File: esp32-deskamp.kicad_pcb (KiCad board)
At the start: 2 copper layers, 140.2 x 66.5 mm, 39 parts, among them J1 INPUT 00, J10 ADDITIONAL GPIO, J2 INPUT 01, J3 MUTE, J4 SLEEP, J5 PRE OUT, J6 LFE OUT, J7 INPUT SELECT, J8 MOTOR, J9 12V IN, K1 INPUT 00, K2 INPUT 01, K3 AMP MUTE, K4 AMP SLEEP, U1 ESP32 D1 MINI, U2 TSR 1-2433, U3 L9110, U4 ULN2003A

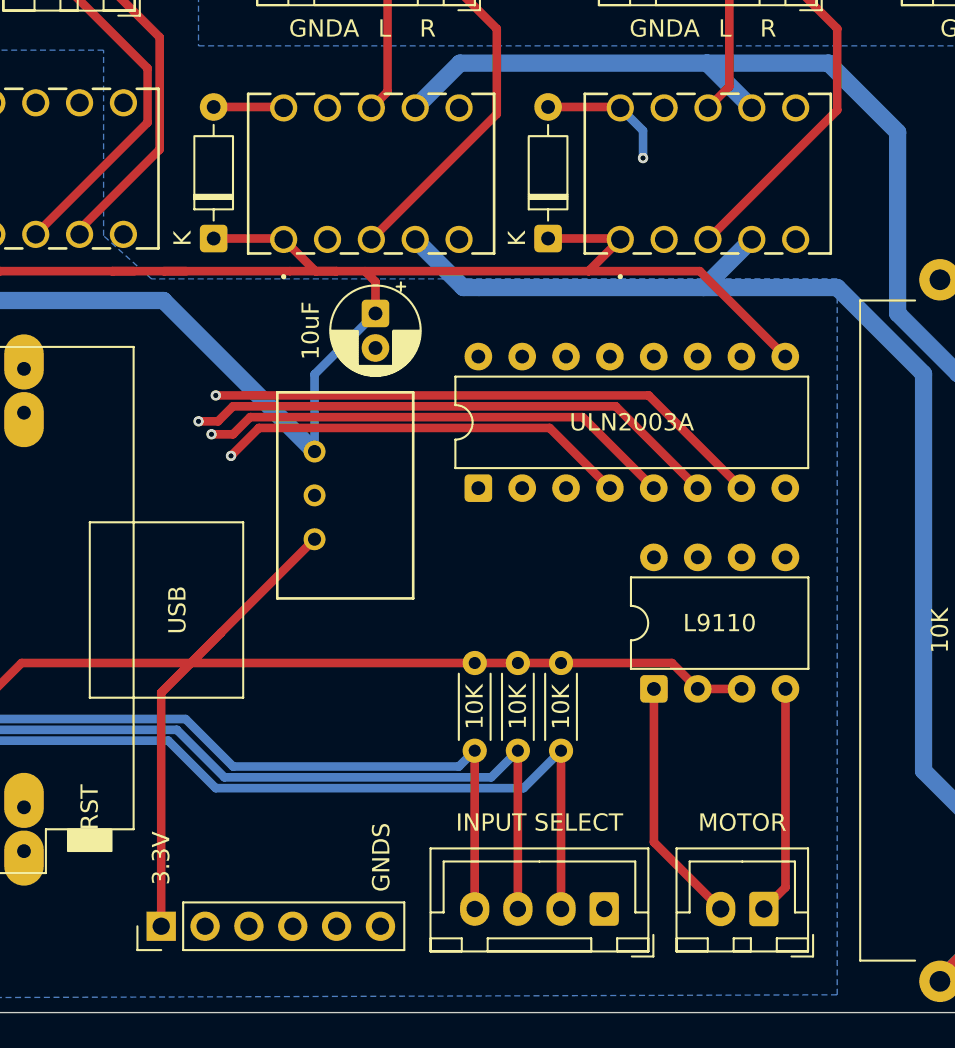
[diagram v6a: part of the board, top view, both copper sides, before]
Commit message: No surprise, more routing (relays)
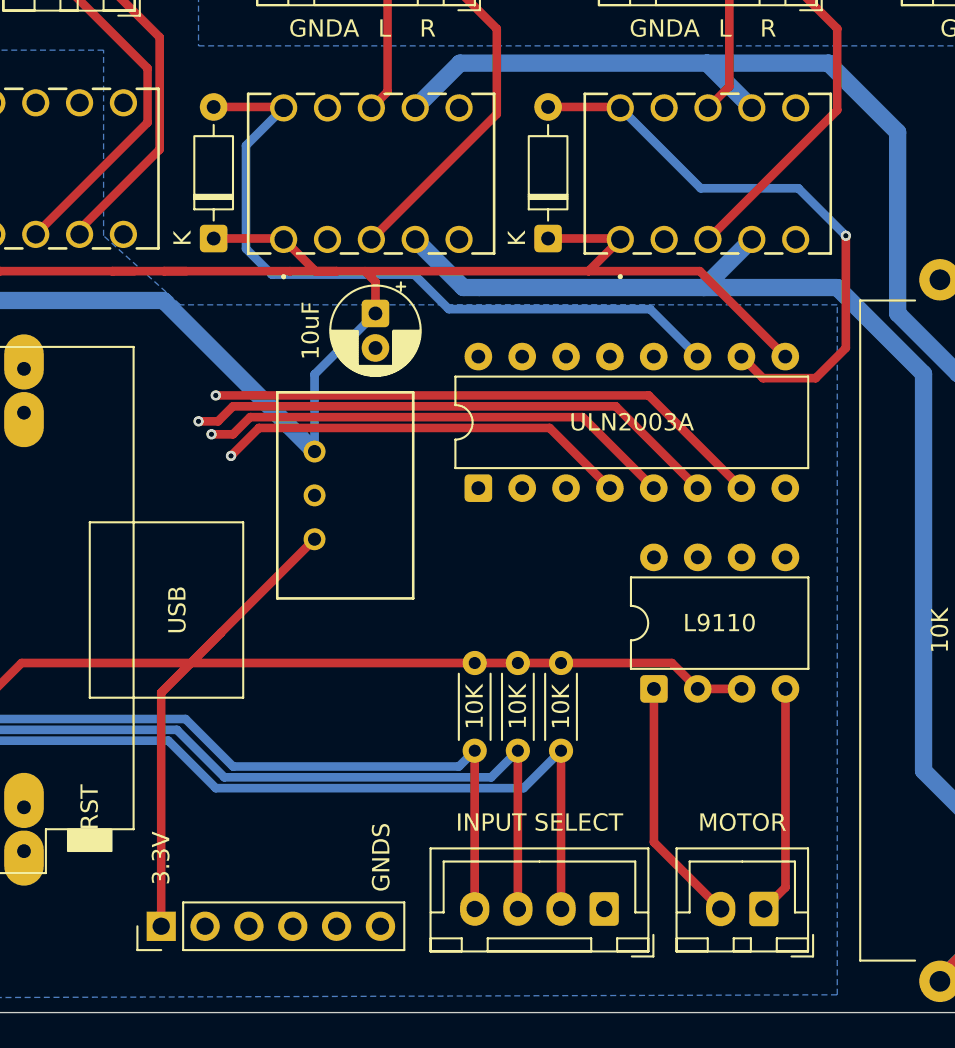
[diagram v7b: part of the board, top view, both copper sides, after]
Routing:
- net Relay0: track 4.00 -> 41.8 mm
- net Relay1: track 7.58 -> 34.1 mm
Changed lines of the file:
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@@
+	)
+	(segment
+		(start 145.5 57.25)
+		(end 147.5 59.25)
+		(width 0.5)
+		(layer "B.Cu")
+		(net 1)
+	)
+	(segment
+		(start 147.5 59.25)
+		(end 159.16 59.25)
+		(width 0.5)
+		(layer "B.Cu")
+		(net 1)
+	)
+	(segment
+		(start 159.16 59.25)
+		(end 161.91 62)
+		(width 0.5)
+		(layer "B.Cu")
+		(net 1)
+	)
+	(segment
+		(start 137.9327 47.5931)
+		(end 135.75 49.7758)
+		(width 0.5)
+		(layer "B.Cu")
+		(net 1)
+	)
+	(segment
+		(start 135.75 49.7758)
+		(end 135.75 55.75)
+		(width 0.5)
+		(layer "B.Cu")
+		(net 1)
+	)
+	(segment
+		(start 135.75 55.75)
+		(end 137.25 57.25)
+		(width 0.5)
+		(layer "B.Cu")
+		(net 1)
+	)
+	(segment
+		(start 137.25 57.25)
+		(end 145.5 57.25)
+		(width 0.5)
+		(layer "B.Cu")
+		(net 1)
 	)
 	(segment
@@
 	)
 	(segment
+		(start 168.749 63.251)
+		(end 165.701 63.251)
+		(width 0.5)
+		(layer "F.Cu")
+		(net 3)
+	)
+	(segment
+		(start 165.701 63.251)
+		(end 164.45 62)
+		(width 0.5)
+		(layer "F.Cu")
+		(net 3)
+	)
+	(segment
+		(start 170.5 55)
+		(end 170.5 61.5)
+		(width 0.5)
+		(layer "F.Cu")
+		(net 3)
+	)
+	(segment
+		(start 170.5 61.5)
+		(end 168.749 63.251)
+		(width 0.5)
+		(layer "F.Cu")
+		(net 3)
+	)
+	(segment
 		(start 153.25 47.54)
 		(end 157.3796 47.54)
@@
 	)
 	(via
-		(at 158.75 50.5)
+		(at 170.5 55)
 		(size 0.6)
 		(drill 0.3)
@@
 	)
 	(segment
-		(start 158.75 50.5)
-		(end 158.75 48.9104)
+		(start 162.0896 52.25)
+		(end 157.4327 47.5931)
 		(width 0.5)
 		(layer "B.Cu")
@@
 	)
 	(segment
-		(start 158.75 48.9104)
-		(end 157.4327 47.5931)
+		(start 167.75 52.25)
+		(end 162.0896 52.25)
+		(width 0.5)
+		(layer "B.Cu")
+		(net 3)
+	)
+	(segment
+		(start 170.5 55)
+		(end 167.75 52.25)
 		(width 0.5)
 		(layer "B.Cu")
@@
 		(min_thickness 0.25)
 		(filled_areas_thickness no)
-		(fill
+		(fill yes
 			(thermal_gap 0.5)
 			(thermal_bridge_width 0.5)
@@
 		(polygon
 			(pts
-				(xy 91.75 34.5) (xy 91.5 68.5) (xy 91.230462 99.227189) (xy 170 98.969772) (xy 170 57.5) (xy 130.277778 57.5)
+				(xy 91.75 34.5) (xy 91.5 68.5) (xy 91.230462 99.227189) (xy 170 98.969772) (xy 170 59) (xy 131.944445 59)
 				(xy 127.5 55) (xy 127.5 44.25) (xy 102.5 44.25) (xy 102.5 34.5)
 			)

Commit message: IC routing
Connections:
- U3 pad 6: PWM1 -> PWM0
- U3 pad 7: PWM0 -> PWM1
- U4 pad 10: Relay1 -> Relay0
- U4 pad 11: Relay0 -> Relay1
- U4 pad 12: Relay3 -> Relay2
- U4 pad 13: Relay2 -> Relay3
- U4 pad 4: Mute -> Sleep
- U4 pad 5: Sleep -> Mute
- U4 pad 6: Input0 -> Input1
- U4 pad 7: Input1 -> Input0
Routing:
- net Relay2: track 4.27 -> 76.3 mm, vias 0 -> 1
- net PWM0: track 0.57 -> 62.6 mm
- net PWM1: track 0.57 -> 62.4 mm
- net Relay3: track 4.32 -> 53.5 mm, vias 0 -> 1
- net Relay0: track 41.8 -> 54.0 mm, vias 0 -> 1
- net Sleep: track 27.7 -> 20.6 mm, vias 1 -> 0
- net Relay1: track 34.1 -> 40.8 mm
- net +3V3: track 83.7 -> 89.3 mm
- net +12V: track 180.0 -> 175.0 mm
- net Input0: track 31.2 -> 34.1 mm, vias 1 -> 0
- net Input1: track 33.2 -> 30.7 mm, vias 1 -> 0
- net Mute: track 24.6 -> 25.8 mm, vias 1 -> 0
- net Net-(J3-Pin_1): track 18.7 -> 19.5 mm
- net Net-(J3-Pin_2): track 18.7 -> 19.5 mm
- net Select2: track 58.8 -> 58.2 mm
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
